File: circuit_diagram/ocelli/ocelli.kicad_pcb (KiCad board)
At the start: 2 copper layers, 80 x 58 mm, 114 parts, among them J1 Conn_01x06, J2 Conn_01x06, J3 Conn_01x06, J4 Conn_01x06, J5 Conn_01x08, J6 Conn_01x02, J7 Conn_01x02, Q1 BSS138, Q10 BSS138, Q2 ST-1KL3A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

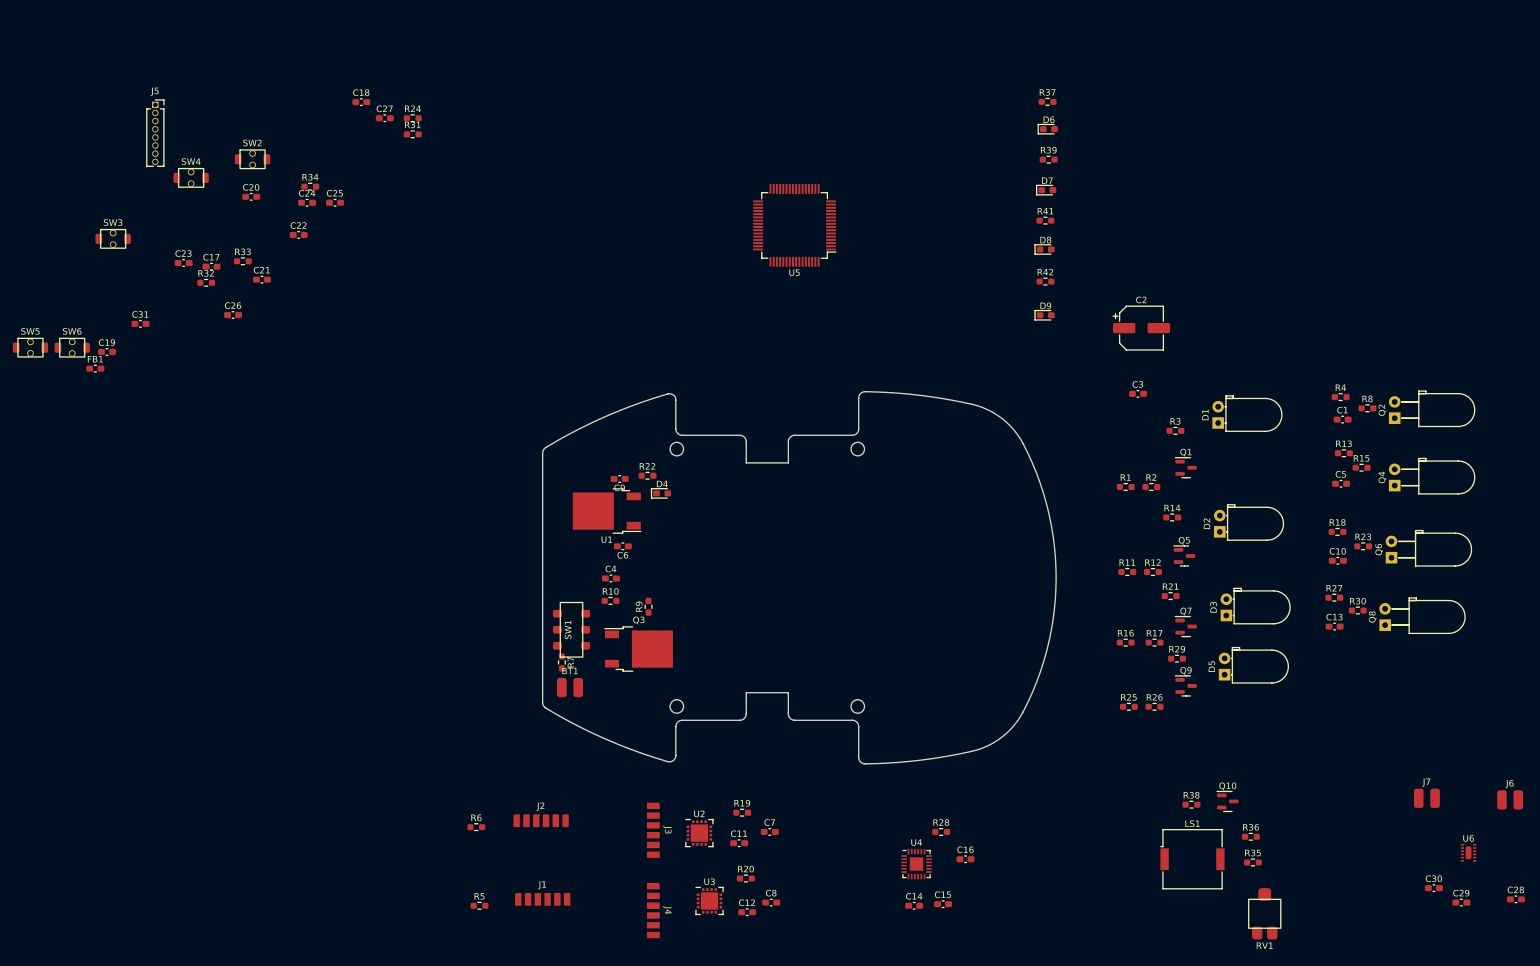
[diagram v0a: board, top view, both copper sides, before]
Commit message: モータマウント等のスケッチ追加
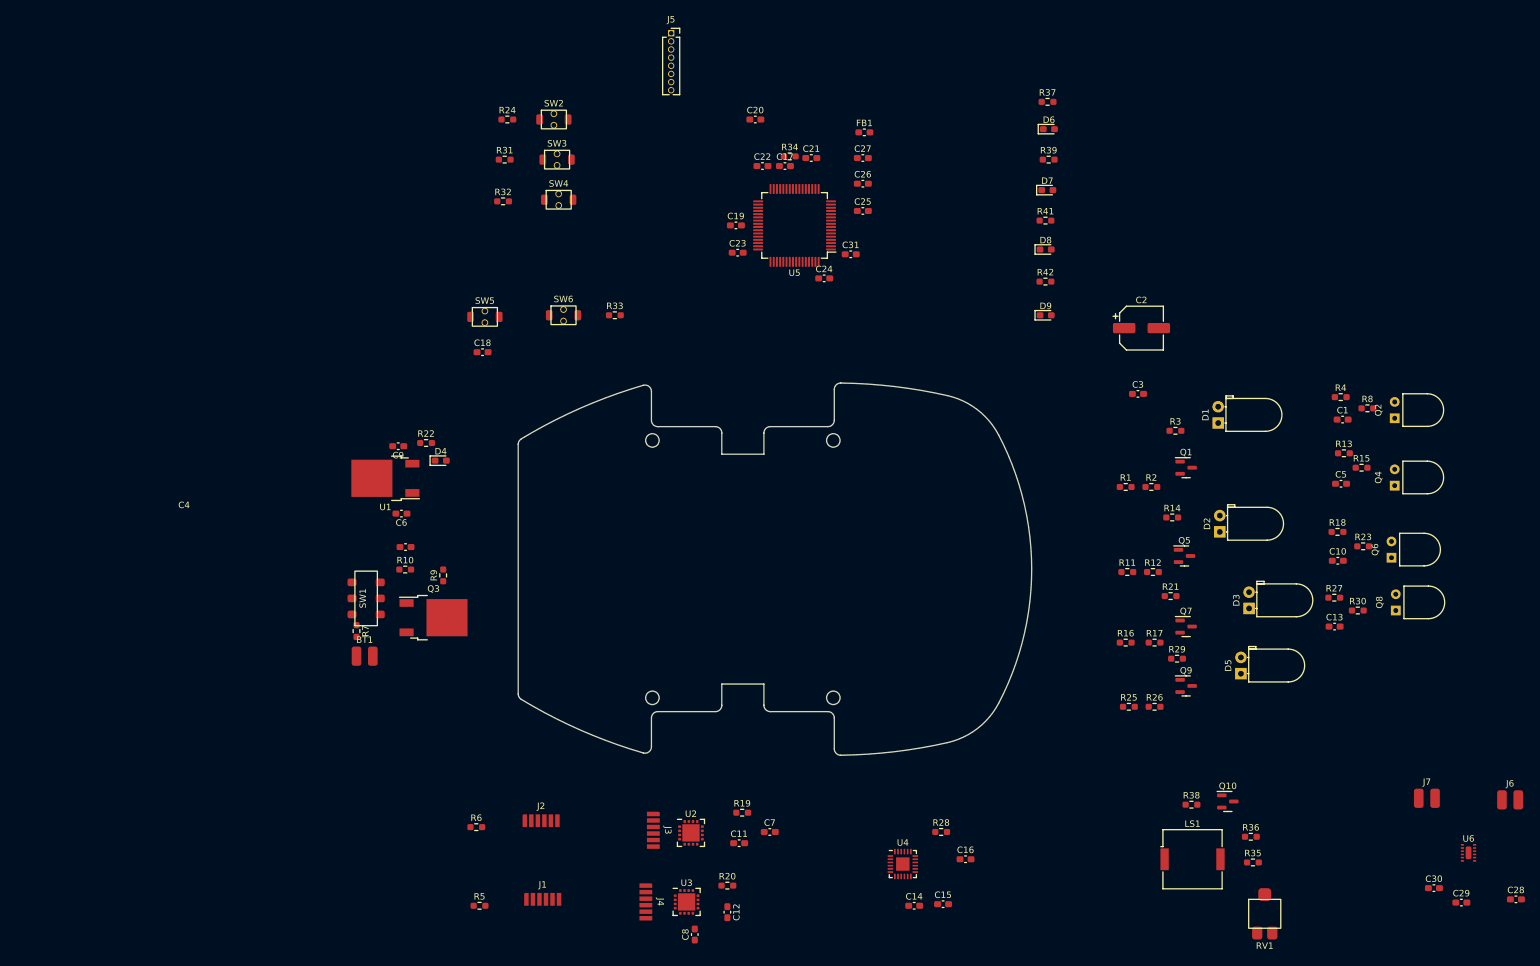
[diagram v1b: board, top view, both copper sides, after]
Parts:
- Q2, Q4, Q6, Q8: footprint LED_THT:LED_D5.0mm_Horizontal_O3.81mm_Z9.0mm -> ocelli_lib:ST-1KL3A
- moved FB1 125.3 mm to (166.1, 32.5)
- moved C31 111.2 mm to (164.0, 51.5)
- moved C26 100.2 mm to (165.9, 40.5)
- moved C19 99.9 mm to (146.1, 47.0)
- moved C17 90.7 mm to (153.8, 37.8)
- moved C21 87.7 mm to (157.9, 36.5)
- moved C23 86.3 mm to (146.4, 51.2)
- moved C25 82.2 mm to (165.9, 44.8)
- moved C24 81.4 mm to (159.9, 55.2)
- moved J5 81.1 mm to (136.0, 17.1)
- moved C20 79.5 mm to (149.1, 30.5)
- moved SW6 76.7 mm to (119.2, 61.0)
- moved R34 74.9 mm to (154.5, 36.2)
- moved C27 74.7 mm to (165.9, 36.5)
- moved C22 73.0 mm to (150.2, 37.8)
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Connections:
- SW2 pad 2: SW_0 -> GND
- SW3 pad 2: SW_1 -> GND
- SW4 pad 2: SW_2 -> GND
